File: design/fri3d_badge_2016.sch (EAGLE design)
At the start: 43 parts, among them U1 MCP73831, Y1 8MHz

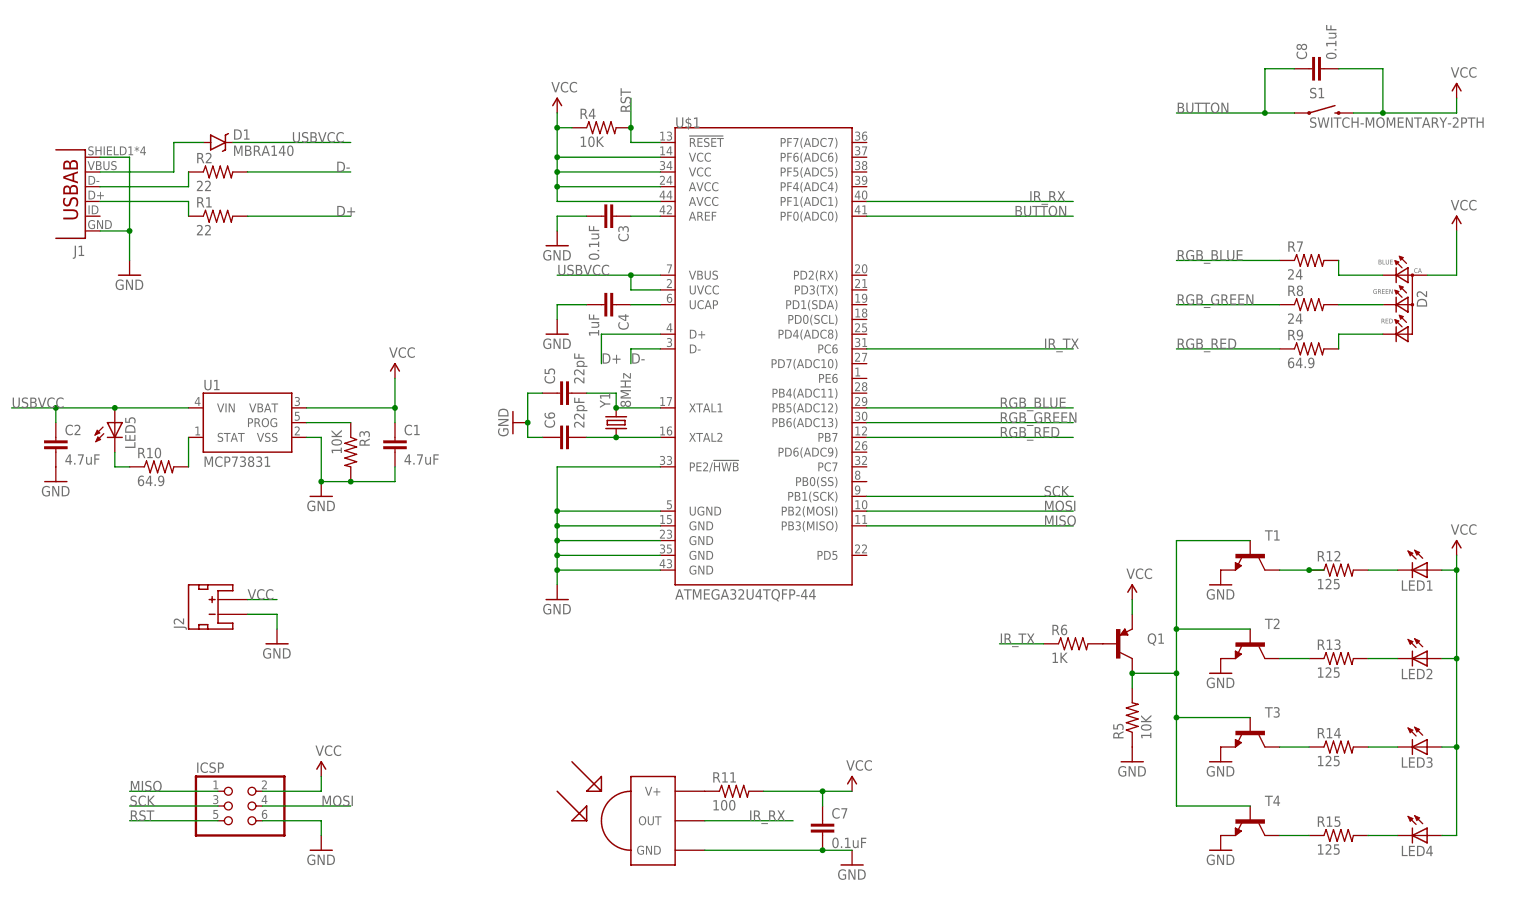
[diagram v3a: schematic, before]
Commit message: update to version 2 of design
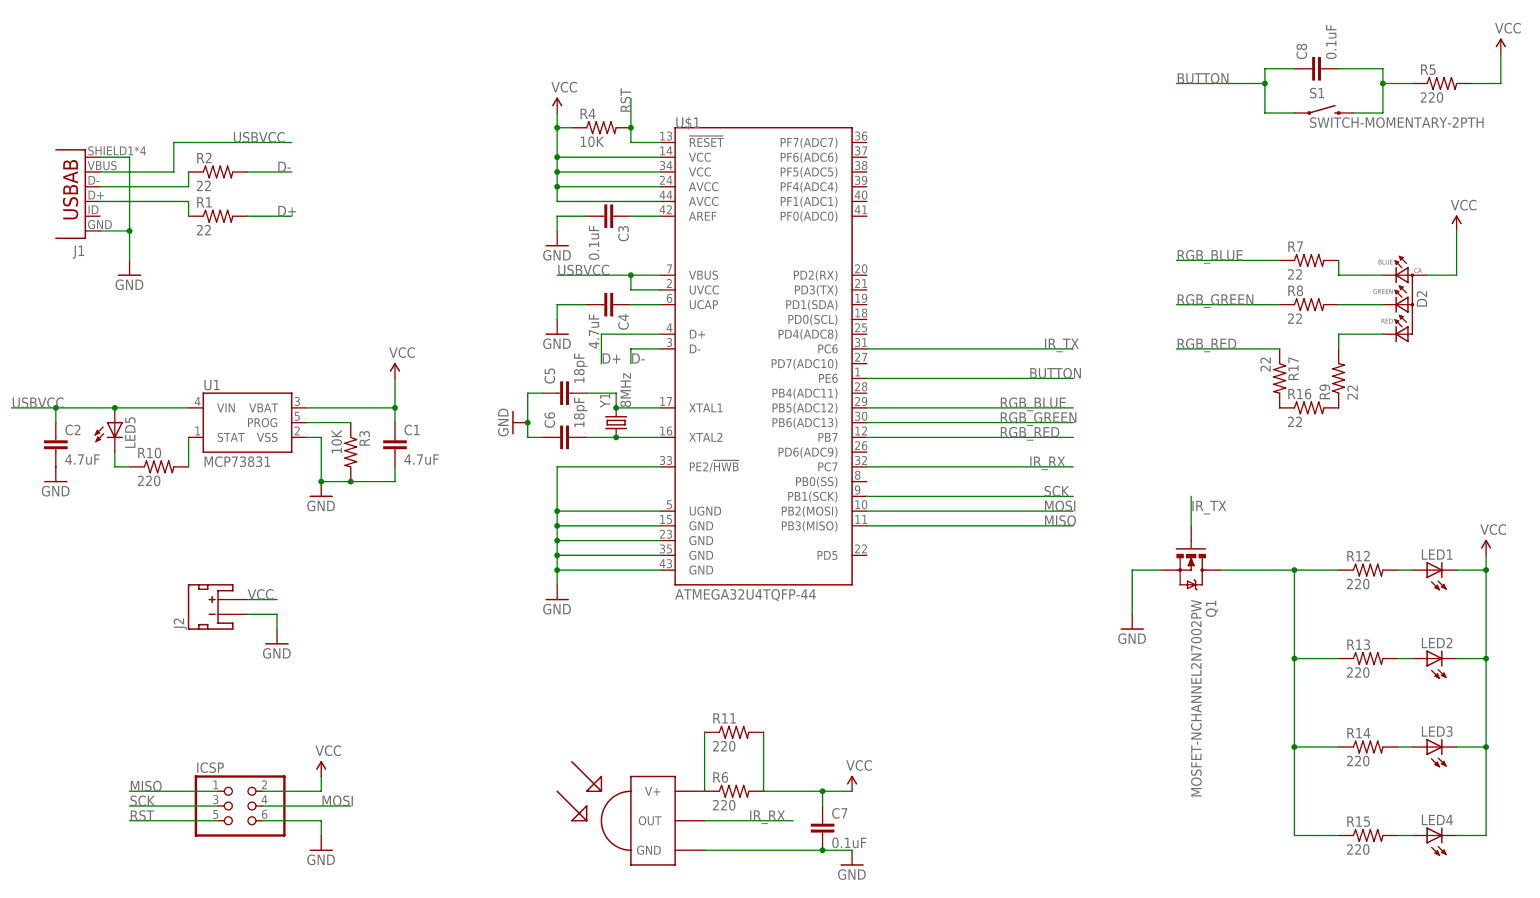
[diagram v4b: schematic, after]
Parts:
- removed D1: MBRA140, SparkFun-DiscreteSemi:DIODE-SCHOTTKY-MBRA140
- removed T1, T2, T3, T4: (no value), transistor-neu-to92:-NPN-SOT223
- added R16, R17: 22, SparkFun-Passives:RESISTOR0805-RES
- C4: value 1uF -> 4.7uF
- C5, C6: value 22pF -> 18pF
- LED1, LED2, LED3, LED4: device led:LEDCHIP-LED0805 -> led:LEDCHIPLED_0805
- Q1: value (none) -> MOSFET-NCHANNEL2N7002PW; device SparkFun-DiscreteSemi:TRANSISTOR_PNPSMD -> SparkFun-DiscreteSemi:MOSFET-NCHANNEL2N7002PW
- R10: value 64.9 -> 220
- R11: value 100 -> 220
- R12, R13, R14, R15: value 125 -> 220
- R5: value 10K -> 220
- R6: value 1K -> 220
- R7, R8: value 24 -> 22
- R9: value 64.9 -> 22
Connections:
- removed net N$17: LED3.C, R14.2
- removed net N$18: R14.1, T3.C
- removed net N$23: LED4.C, R15.2
- net BUTTON: now also U$1.PE6; no longer U$1.PF0(ADC0)
- net GND: now also Q1.S; no longer R5.1, T1.E, T2.E, T3.E, T4.E
- net IR_RX: now also U$1.PC7; no longer U$1.PF1(ADC1)
- net IR_TX: now also Q1.G; no longer R6.1
- net N$10: now also R11.1, R6.1, U$3.V+; no longer Q1.C, R5.2, T1.B, T2.B, T3.B, T4.B
- net N$11: now also R16.2, R9.1; no longer Q1.B, R6.2
- net N$12: now also R16.1, R17.2; no longer R12.1, T1.C
- net N$13: now also LED1.A; no longer LED1.C
- net N$14: now also LED2.A; no longer LED2.C
- net N$15: now also LED3.A, R14.2; no longer R13.1, T2.C
- net N$16: now also LED4.A, R15.2; no longer R11.1, U$3.V+
- net N$24: now also Q1.D, R12.1, R13.1, R14.1; no longer T4.C
- net N$3: now also C8.2, R5.1, S1.2; no longer D1.A, J1.VBUS
- net RGB_RED: now also R17.1; no longer R9.1
- net USBVCC: now also J1.VBUS; no longer D1.C
- net VCC: now also LED1.C, LED2.C, LED3.C, LED4.C, R5.2, R6.2; no longer C8.2, LED1.A, LED2.A, LED3.A, LED4.A, Q1.E, S1.2
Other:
- moved on the sheet: LED1, LED2, LED3, LED4, R11, R12, R13, R14, R15, R5, R6, R9

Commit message: created first version (draft) PCB layout
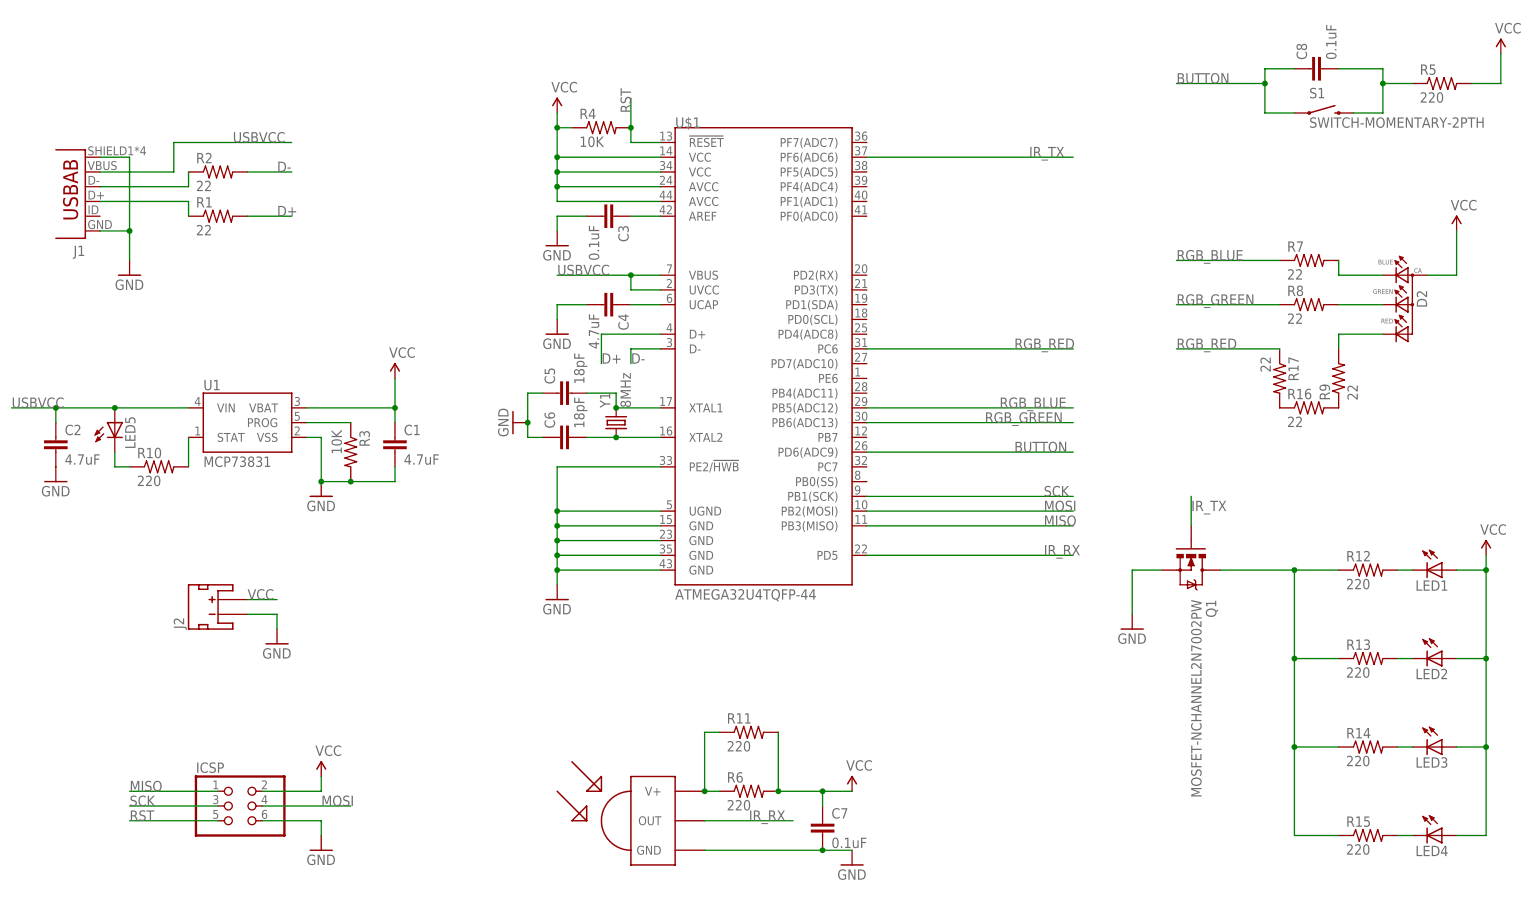
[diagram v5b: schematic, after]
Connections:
- net BUTTON: now also U$1.PD6(ADC9); no longer U$1.PE6
- net IR_RX: now also U$1.PD5; no longer U$1.PC7
- net IR_TX: now also U$1.PF6(ADC6); no longer U$1.PC6
- net N$13: now also LED1.C; no longer LED1.A
- net N$14: now also LED2.C; no longer LED2.A
- net N$15: now also LED3.C; no longer LED3.A
- net N$16: now also LED4.C; no longer LED4.A
- net RGB_RED: now also U$1.PC6; no longer U$1.PB7
- net VCC: now also LED1.A, LED2.A, LED3.A, LED4.A; no longer LED1.C, LED2.C, LED3.C, LED4.C
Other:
- moved on the sheet: LED1, LED2, LED3, LED4, R11, R6
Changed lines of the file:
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@@
 <instance part="Q1" gate="G$1" x="162.56" y="71.12" rot="R270"/>
 <instance part="R5" gate="G$1" x="205.74" y="154.94"/>
-<instance part="R6" gate="G$1" x="83.82" y="33.02"/>
-<instance part="R11" gate="G$1" x="83.82" y="43.18"/>
+<instance part="R6" gate="G$1" x="86.36" y="33.02"/>
+<instance part="R11" gate="G$1" x="86.36" y="43.18"/>
 <instance part="R9" gate="G$1" x="187.96" y="104.14" rot="R90"/>
 <instance part="R16" gate="G$1" x="182.88" y="99.06"/>
 <instance part="R17" gate="G$1" x="177.8" y="104.14" rot="R270"/>
-<instance part="LED1" gate="G$1" x="203.2" y="71.12" rot="R90"/>
-<instance part="LED2" gate="G$1" x="203.2" y="55.88" rot="R90"/>
-<instance part="LED3" gate="G$1" x="203.2" y="40.64" rot="R90"/>
-<instance part="LED4" gate="G$1" x="203.2" y="25.4" rot="R90"/>
+<instance part="LED1" gate="G$1" x="205.74" y="71.12" rot="R270"/>
+<instance part="LED2" gate="G$1" x="205.74" y="55.88" rot="R270"/>
+<instance part="LED3" gate="G$1" x="205.74" y="40.64" rot="R270"/>
+<instance part="LED4" gate="G$1" x="205.74" y="25.4" rot="R270"/>
 </instances>
 <busses>
@@
 </segment>
 <segment>
+<wire x1="12.7" y1="27.94" x2="12.7" y2="25.4" width="0.1524" layer="91"/>
+<pinref part="GND18" gate="1" pin="GND"/>
 <pinref part="ICSP" gate="A" pin="6"/>
 <wire x1="2.54" y1="27.94" x2="12.7" y2="27.94" width="0.1524" layer="91"/>
-<wire x1="12.7" y1="27.94" x2="12.7" y2="25.4" width="0.1524" layer="91"/>
-<pinref part="GND18" gate="1" pin="GND"/>
 </segment>
 <segment>
@@
 <segment>
 <pinref part="SUPPLY4" gate="G$1" pin="VCC"/>
+<wire x1="213.36" y1="25.4" x2="213.36" y2="40.64" width="0.1524" layer="91"/>
+<pinref part="LED4" gate="G$1" pin="A"/>
+<wire x1="213.36" y1="40.64" x2="213.36" y2="55.88" width="0.1524" layer="91"/>
+<wire x1="213.36" y1="55.88" x2="213.36" y2="71.12" width="0.1524" layer="91"/>
 <wire x1="213.36" y1="71.12" x2="213.36" y2="73.66" width="0.1524" layer="91"/>
 <wire x1="208.28" y1="25.4" x2="213.36" y2="25.4" width="0.1524" layer="91"/>
-<wire x1="213.36" y1="25.4" x2="213.36" y2="40.64" width="0.1524" layer="91"/>
+<pinref part="LED3" gate="G$1" pin="A"/>
+<wire x1="208.28" y1="40.64" x2="213.36" y2="40.64" width="0.1524" layer="91"/>
+<junction x="213.36" y="40.64"/>
+<pinref part="LED2" gate="G$1" pin="A"/>
+<wire x1="208.28" y1="55.88" x2="213.36" y2="55.88" width="0.1524" layer="91"/>
+<junction x="213.36" y="55.88"/>
+<pinref part="LED1" gate="G$1" pin="A"/>
+<wire x1="208.28" y1="71.12" x2="213.36" y2="71.12" width="0.1524" layer="91"/>
 <junction x="213.36" y="71.12"/>
-<wire x1="213.36" y1="40.64" x2="213.36" y2="55.88" width="0.1524" layer="91"/>
-<wire x1="213.36" y1="55.88" x2="213.36" y2="71.12" width="0.1524" layer="91"/>
-<junction x="213.36" y="55.88"/>
-<junction x="213.36" y="40.64"/>
-<pinref part="LED1" gate="G$1" pin="C"/>
-<wire x1="208.28" y1="71.12" x2="213.36" y2="71.12" width="0.1524" layer="91"/>
-<pinref part="LED2" gate="G$1" pin="C"/>
-<wire x1="208.28" y1="55.88" x2="213.36" y2="55.88" width="0.1524" layer="91"/>
-<pinref part="LED3" gate="G$1" pin="C"/>
-<wire x1="213.36" y1="40.64" x2="208.28" y2="40.64" width="0.1524" layer="91"/>
-<pinref part="LED4" gate="G$1" pin="C"/>
 </segment>
 <segment>
@@
 <wire x1="104.14" y1="33.02" x2="99.06" y2="33.02" width="0.1524" layer="91"/>
 <pinref part="C7" gate="G$1" pin="1"/>
-<wire x1="99.06" y1="33.02" x2="88.9" y2="33.02" width="0.1524" layer="91"/>
 <wire x1="99.06" y1="30.48" x2="99.06" y2="33.02" width="0.1524" layer="91"/>
+<pinref part="R11" gate="G$1" pin="2"/>
+<pinref part="R6" gate="G$1" pin="2"/>
+<wire x1="91.44" y1="43.18" x2="91.44" y2="33.02" width="0.1524" layer="91"/>
+<wire x1="91.44" y1="33.02" x2="99.06" y2="33.02" width="0.1524" layer="91"/>
+<junction x="91.44" y="33.02"/>
 <junction x="99.06" y="33.02"/>
-<pinref part="R6" gate="G$1" pin="2"/>
-<pinref part="R11" gate="G$1" pin="2"/>
-<wire x1="88.9" y1="33.02" x2="88.9" y2="43.18" width="0.1524" layer="91"/>
 </segment>
 <segment>
@@
 </segment>
 <segment>
-<pinref part="U$1" gate="G$1" pin="PC6"/>
-<wire x1="106.68" y1="109.22" x2="142.24" y2="109.22" width="0.1524" layer="91"/>
-<label x="137.16" y="109.22" size="1.778" layer="95"/>
+<pinref part="U$1" gate="G$1" pin="PF6(ADC6)"/>
+<wire x1="106.68" y1="142.24" x2="142.24" y2="142.24" width="0.1524" layer="91"/>
+<label x="134.62" y="142.24" size="1.778" layer="95"/>
 </segment>
 </net>
@@
 </segment>
 <segment>
-<pinref part="U$1" gate="G$1" pin="PE6"/>
-<wire x1="106.68" y1="104.14" x2="142.24" y2="104.14" width="0.1524" layer="91"/>
-<label x="134.62" y="104.14" size="1.778" layer="95"/>
+<pinref part="U$1" gate="G$1" pin="PD6(ADC9)"/>
+<wire x1="106.68" y1="91.44" x2="142.24" y2="91.44" width="0.1524" layer="91"/>
+<label x="132.08" y="91.44" size="1.778" layer="95"/>
 </segment>
 </net>
@@
 <net name="RGB_BLUE" class="0">
 <segment>
+<pinref part="R7" gate="G$1" pin="1"/>
+<wire x1="177.8" y1="124.46" x2="160.02" y2="124.46" width="0.1524" layer="91"/>
+<label x="160.02" y="124.46" size="1.778" layer="95"/>
+</segment>
+<segment>
 <pinref part="U$1" gate="G$1" pin="PB5(ADC12)"/>
 <wire x1="106.68" y1="99.06" x2="142.24" y2="99.06" width="0.1524" layer="91"/>
 <label x="129.54" y="99.06" size="1.778" layer="95"/>
 </segment>
-<segment>
-<pinref part="R7" gate="G$1" pin="1"/>
-<wire x1="177.8" y1="124.46" x2="160.02" y2="124.46" width="0.1524" layer="91"/>
-<label x="160.02" y="124.46" size="1.778" layer="95"/>
-</segment>
 </net>
 <net name="RGB_GREEN" class="0">
-<segment>
-<pinref part="U$1" gate="G$1" pin="PB6(ADC13)"/>
-<wire x1="106.68" y1="96.52" x2="142.24" y2="96.52" width="0.1524" layer="91"/>
-<label x="129.54" y="96.52" size="1.778" layer="95"/>
-</segment>
 <segment>
 <pinref part="R8" gate="G$1" pin="1"/>
@@
 <label x="160.02" y="116.84" size="1.778" layer="95"/>
 </segment>
+<segment>
+<pinref part="U$1" gate="G$1" pin="PB6(ADC13)"/>
+<wire x1="106.68" y1="96.52" x2="142.24" y2="96.52" width="0.1524" layer="91"/>
+<label x="127" y="96.52" size="1.778" layer="95"/>
+</segment>
 </net>
 <net name="RGB_RED" class="0">
-<segment>
-<pinref part="U$1" gate="G$1" pin="PB7"/>
-<wire x1="106.68" y1="93.98" x2="142.24" y2="93.98" width="0.1524" layer="91"/>
-<label x="129.54" y="93.98" size="1.778" layer="95"/>
-</segment>
 <segment>
 <wire x1="177.8" y1="109.22" x2="160.02" y2="109.22" width="0.1524" layer="91"/>
@@
 <pinref part="R17" gate="G$1" pin="1"/>
 </segment>
+<segment>
+<pinref part="U$1" gate="G$1" pin="PC6"/>
+<wire x1="106.68" y1="109.22" x2="142.24" y2="109.22" width="0.1524" layer="91"/>
+<label x="132.08" y="109.22" size="1.778" layer="95"/>
+</segment>
 </net>
 <net name="N$20" class="0">
@@
 </segment>
 <segment>
-<pinref part="U$1" gate="G$1" pin="PC7"/>
-<wire x1="106.68" y1="88.9" x2="142.24" y2="88.9" width="0.1524" layer="91"/>
-<label x="134.62" y="88.9" size="1.778" layer="95"/>
+<pinref part="U$1" gate="G$1" pin="PD5"/>
+<wire x1="106.68" y1="73.66" x2="142.24" y2="73.66" width="0.1524" layer="91"/>
+<label x="137.16" y="73.66" size="1.778" layer="95"/>
 </segment>
 </net>
@@
 <pinref part="U$3" gate="G$1" pin="V+"/>
 <pinref part="R6" gate="G$1" pin="1"/>
+<wire x1="81.28" y1="33.02" x2="78.74" y2="33.02" width="0.1524" layer="91"/>
 <pinref part="R11" gate="G$1" pin="1"/>
-<wire x1="78.74" y1="33.02" x2="78.74" y2="43.18" width="0.1524" layer="91"/>
+<wire x1="81.28" y1="43.18" x2="78.74" y2="43.18" width="0.1524" layer="91"/>
+<wire x1="78.74" y1="43.18" x2="78.74" y2="33.02" width="0.1524" layer="91"/>
+<junction x="78.74" y="33.02"/>
 </segment>
 </net>
@@
 <segment>
 <pinref part="R12" gate="G$1" pin="2"/>
-<pinref part="LED1" gate="G$1" pin="A"/>
-<wire x1="198.12" y1="71.12" x2="200.66" y2="71.12" width="0.1524" layer="91"/>
+<pinref part="LED1" gate="G$1" pin="C"/>
+<wire x1="200.66" y1="71.12" x2="198.12" y2="71.12" width="0.1524" layer="91"/>
 </segment>
 </net>
@@
 <segment>
 <pinref part="R13" gate="G$1" pin="2"/>
-<pinref part="LED2" gate="G$1" pin="A"/>
-<wire x1="198.12" y1="55.88" x2="200.66" y2="55.88" width="0.1524" layer="91"/>
+<pinref part="LED2" gate="G$1" pin="C"/>
+<wire x1="200.66" y1="55.88" x2="198.12" y2="55.88" width="0.1524" layer="91"/>
 </segment>
 </net>
 <net name="N$15" class="0">
 <segment>
-<pinref part="LED3" gate="G$1" pin="A"/>
 <pinref part="R14" gate="G$1" pin="2"/>
+<pinref part="LED3" gate="G$1" pin="C"/>
 <wire x1="200.66" y1="40.64" x2="198.12" y2="40.64" width="0.1524" layer="91"/>
 </segment>
@@
 <segment>
 <pinref part="R15" gate="G$1" pin="2"/>
-<pinref part="LED4" gate="G$1" pin="A"/>
-<wire x1="198.12" y1="25.4" x2="200.66" y2="25.4" width="0.1524" layer="91"/>
-</segment>
-</net>
+<pinref part="LED4" gate="G$1" pin="C"/>
+<wire x1="200.66" y1="25.4" x2="198.12" y2="25.4" width="0.1524" layer="91"/>
+</segment>
+</net>
